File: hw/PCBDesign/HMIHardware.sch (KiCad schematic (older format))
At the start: 24 parts

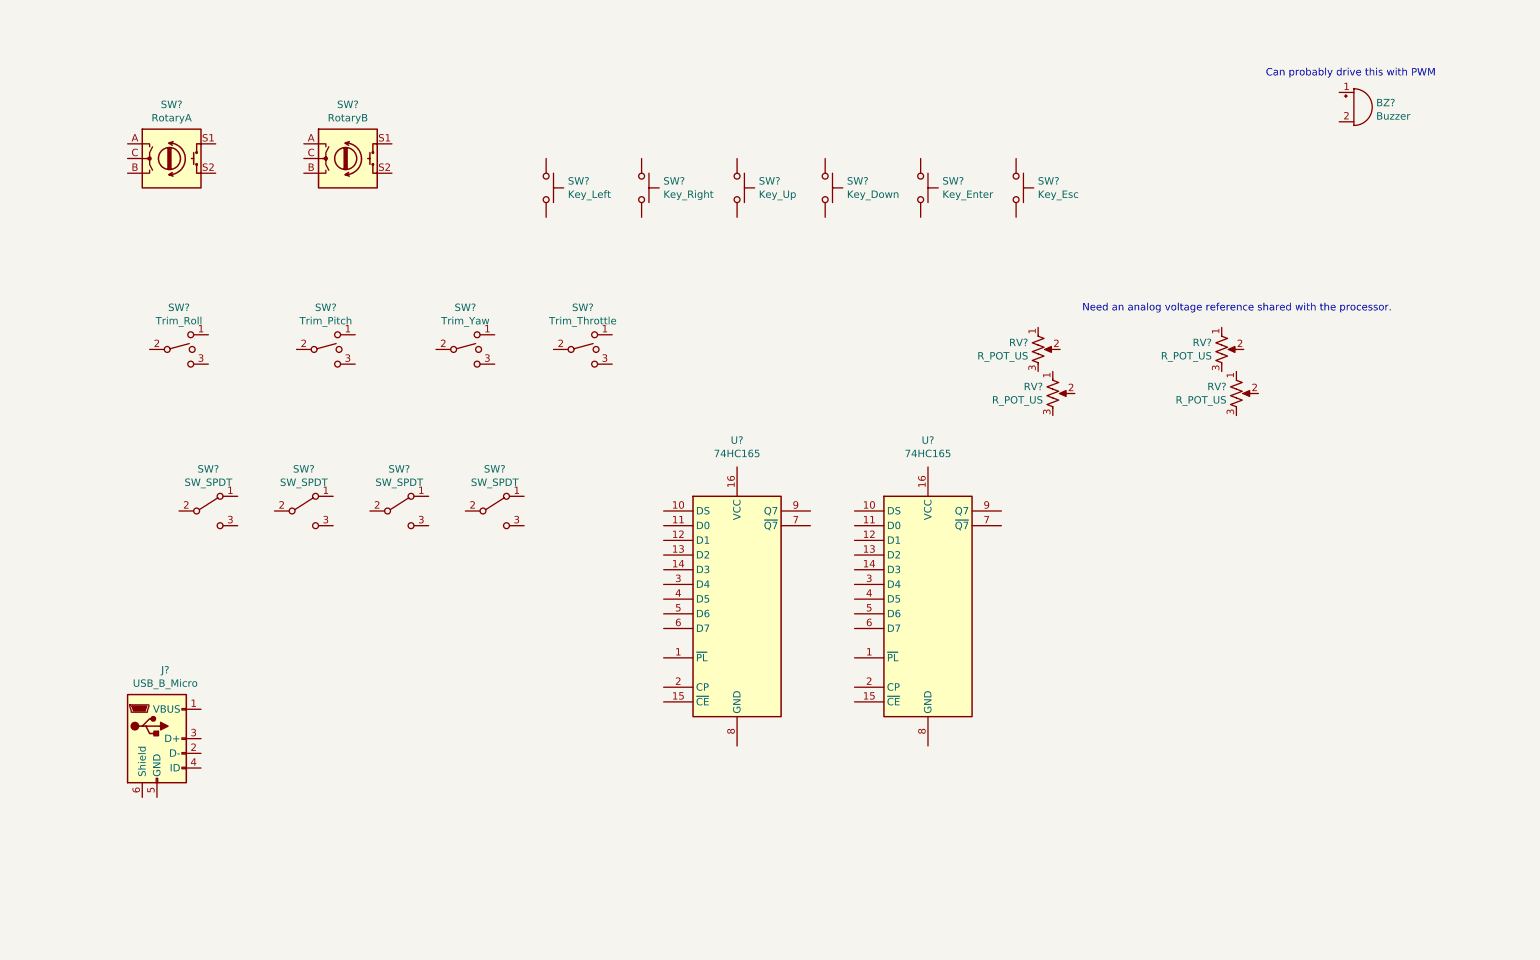
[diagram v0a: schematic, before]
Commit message: Fill out a lot of the board schematic
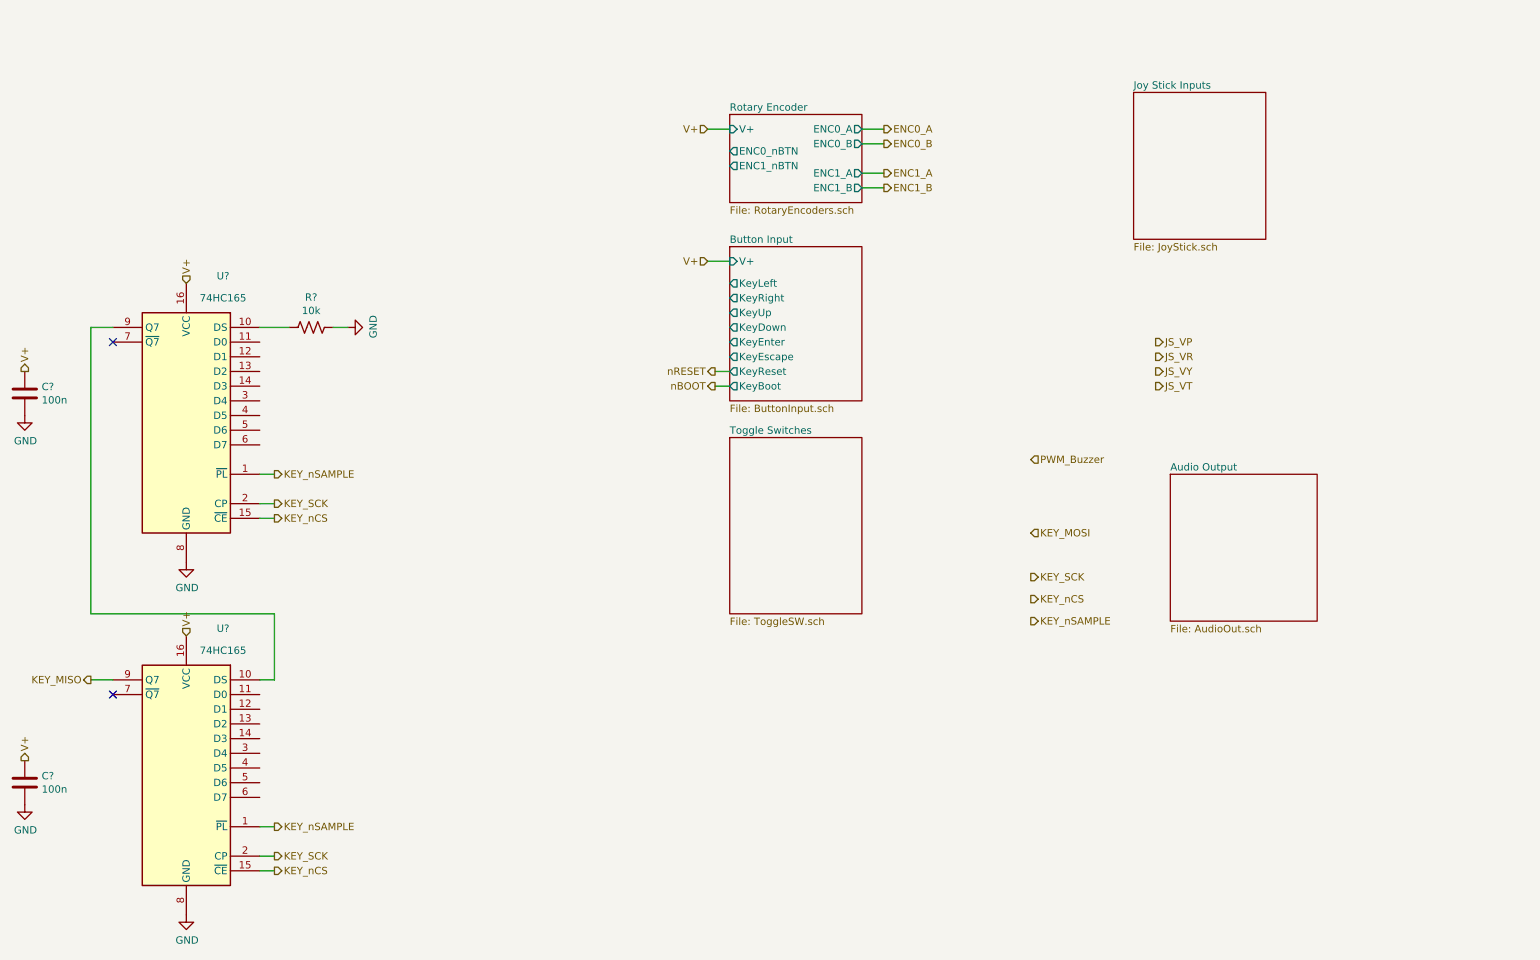
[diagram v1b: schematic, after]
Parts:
- removed BZ?: Buzzer, symbol Device:Buzzer
- removed J?: USB_B_Micro, symbol Connector:USB_B_Micro
- removed RV? (x4): R_POT_US, symbol Device:R_POT_US
- removed SW?: RotaryA, symbol Device:Rotary_Encoder_Switch
- removed SW?: RotaryB, symbol Device:Rotary_Encoder_Switch
- removed SW?: Trim_Roll, symbol Switch:SW_SPDT_MSM
- removed SW?: Trim_Pitch, symbol Switch:SW_SPDT_MSM
- removed SW?: Trim_Yaw, symbol Switch:SW_SPDT_MSM
- removed SW?: Trim_Throttle, symbol Switch:SW_SPDT_MSM
- removed SW?: Key_Left, symbol Switch:SW_Push
- removed SW?: Key_Right, symbol Switch:SW_Push
- removed SW?: Key_Up, symbol Switch:SW_Push
- removed SW?: Key_Down, symbol Switch:SW_Push
- removed SW?: Key_Enter, symbol Switch:SW_Push
- removed SW?: Key_Esc, symbol Switch:SW_Push
- removed SW? (x4): SW_SPDT, symbol Switch:SW_SPDT
- added C? (x2): 100n, symbol Device:C
- added R?: 10k, symbol Device:R_US
- U? (x2): footprint (none) -> Package_SO:SOIC-16_3.9x9.9mm_P1.27mm; LCSC (none) -> C5613
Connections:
- net KEY_nSAMPLE: now reaches U?.1 (~PL)
- net KEY_nSAMPLE: now also U?.1 (~PL)
- net at U?.10 (DS): now also R?.1
- net KEY_nCS: now reaches U?.15 (~CE)
- net KEY_nCS: now also U?.15 (~CE)
- net V+: now reaches U?.16 (VCC)
- net V+: now also U?.16 (VCC), C?.1, C?.1
- net KEY_SCK: now reaches U?.2 (CP)
- net KEY_SCK: now also U?.2 (CP)
- net GND: now reaches U?.8 (GND)
- net GND: now also U?.8 (GND), C?.2, C?.2, R?.2
- net at U?.9 (Q7): now also U?.10 (DS)
- net KEY_MISO: now reaches U?.9 (Q7)
- no-connect marks 0 -> 2
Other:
- note removed: "Can probably drive this with PWM\n"
- note removed: "Need an analog voltage reference shared with the processor."
- moved on the sheet: U?

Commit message: Add HMI input circuitry
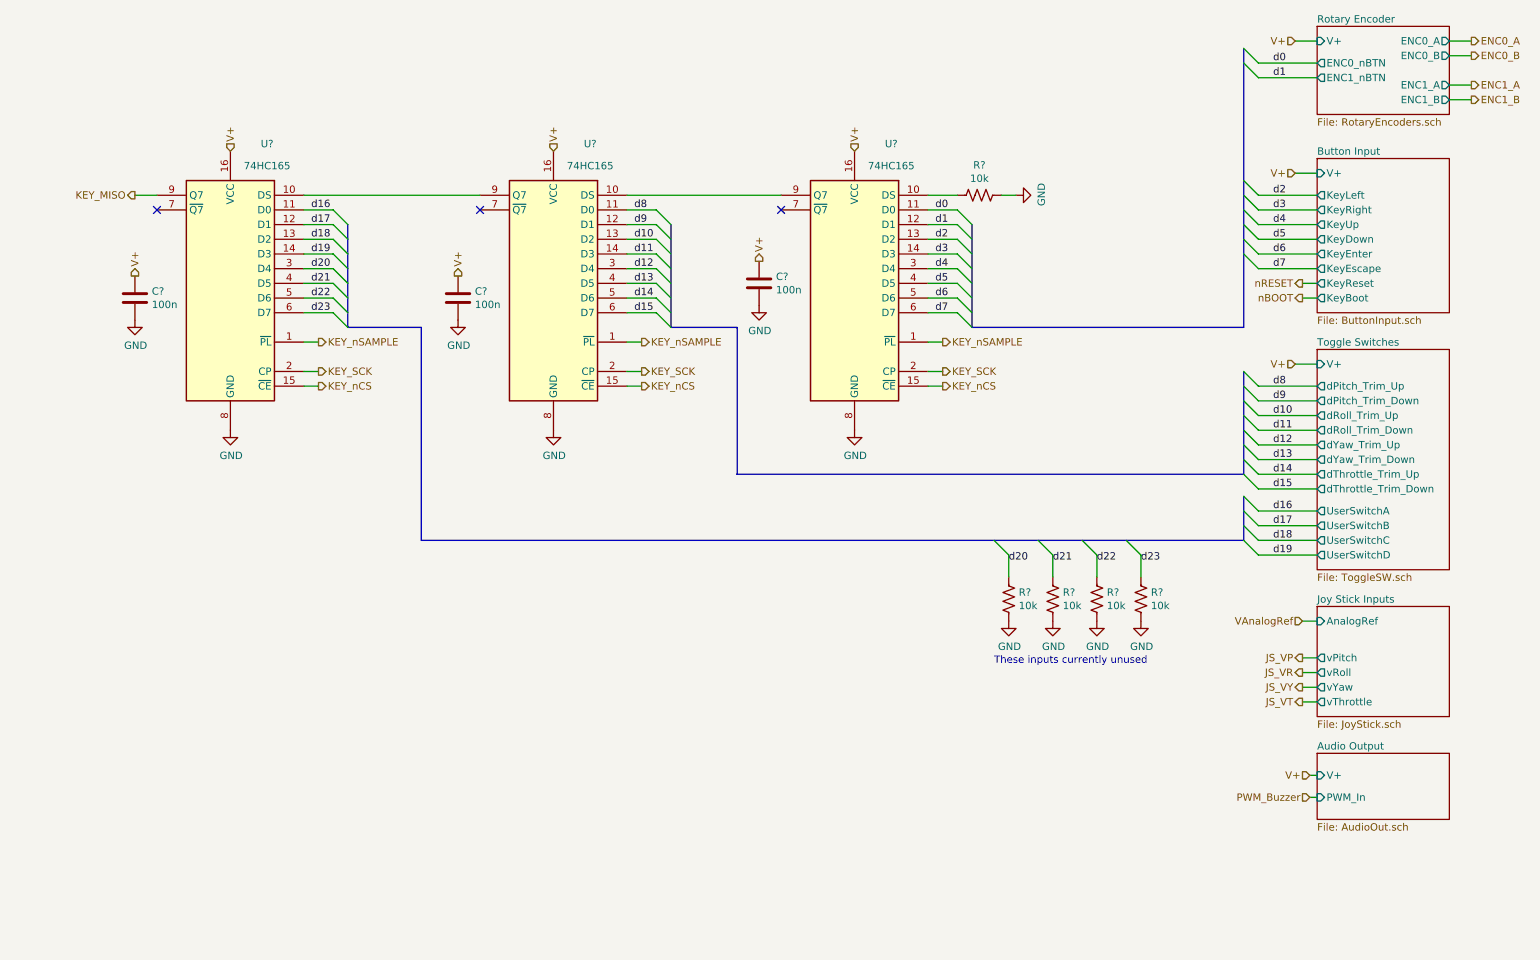
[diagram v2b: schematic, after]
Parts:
- added C?: 100n, symbol Device:C
- added R? (x4): 10k, symbol Device:R_US
- added U?: 74HC165, Package_SO:SOIC-16_3.9x9.9mm_P1.27mm, symbol 74xx:74HC165
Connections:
- net GND: now also C?.2, R?.2, R?.2, R?.2, R?.2, U?.8 (GND)
- net KEY_SCK: now also U?.2 (CP)
- net KEY_nCS: now also U?.15 (~CE)
- net KEY_nSAMPLE: now also U?.1 (~PL)
- net V+: now also C?.1, U?.16 (VCC)
- net d0: now reaches U?.11 (D0)
- net d1: now reaches U?.12 (D1)
- net d2: now reaches U?.13 (D2)
- net d3: now reaches U?.14 (D3)
- net d4: now reaches U?.3 (D4)
- net d5: now reaches U?.4 (D5)
- net d6: now reaches U?.5 (D6)
- net d7: now reaches U?.6 (D7)
- net at U?.9 (Q7): now also U?.10 (DS); no longer U?.10 (DS)
- net d16: now reaches U?.11 (D0)
- net d17: now reaches U?.12 (D1)
- net d18: now reaches U?.13 (D2)
- net d19: now reaches U?.14 (D3)
- net d20: now reaches U?.3 (D4)
- net d20: now also R?.1
- net d21: now reaches U?.4 (D5)
- net d21: now also R?.1
- net d22: now reaches U?.5 (D6)
- net d22: now also R?.1
- net d23: now reaches U?.6 (D7)
- net d23: now also R?.1
- new net: U?.10 (DS), U?.9 (Q7)
- new net d10: U?.13 (D2)
- new net d11: U?.14 (D3)
- new net d12: U?.3 (D4)
- new net d13: U?.4 (D5)
- new net d14: U?.5 (D6)
- new net d15: U?.6 (D7)
- new net d8: U?.11 (D0)
- new net d9: U?.12 (D1)
- no-connect marks 2 -> 3
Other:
- note added: "These inputs currently unused"
- moved on the sheet: C?, R?, U?

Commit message: Finished initial schematic design
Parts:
- removed R? (x2): 10k, symbol Device:R_US
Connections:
- net d20 renamed nBatteryPowerGood
- net d21 renamed nBatteryChargeGood
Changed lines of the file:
@@
-$Comp
-L Device:R_US R?
-U 1 1 605874BC
-P 7500 4650
-F 0 "R?" H 7568 4696 50  0000 L CNN
-F 1 "10k" H 7568 4605 50  0000 L CNN
-F 2 "" V 7540 4640 50  0001 C CNN
-F 3 "~" H 7500 4650 50  0001 C CNN
-	1    7500 4650
-	1    0    0    -1
-$EndComp
-$Comp
-L Device:R_US R?
-U 1 1 60587B6F
-P 7800 4650
-F 0 "R?" H 7868 4696 50  0000 L CNN
-F 1 "10k" H 7868 4605 50  0000 L CNN
-F 2 "" V 7840 4640 50  0001 C CNN
-F 3 "~" H 7800 4650 50  0001 C CNN
-	1    7800 4650
-	1    0    0    -1
-$EndComp
 $Comp
 L Device:R_US R?
@@
 F 3 "~" H 8400 4650 50  0001 C CNN
 	1    8400 4650
-	1    0    0    -1
-$EndComp
-$Comp
-L power:GND #PWR?
-U 1 1 6058901C
-P 7500 4800
-F 0 "#PWR?" H 7500 4550 50  0001 C CNN
-F 1 "GND" H 7505 4627 50  0000 C CNN
-F 2 "" H 7500 4800 50  0001 C CNN
-F 3 "" H 7500 4800 50  0001 C CNN
-	1    7500 4800
-	1    0    0    -1
-$EndComp
-$Comp
-L power:GND #PWR?
-U 1 1 6058949C
-P 7800 4800
-F 0 "#PWR?" H 7800 4550 50  0001 C CNN
-F 1 "GND" H 7805 4627 50  0000 C CNN
-F 2 "" H 7800 4800 50  0001 C CNN
-F 3 "" H 7800 4800 50  0001 C CNN
-	1    7800 4800
 	1    0    0    -1
 $EndComp
@@
 Text Label 8400 4400 0    50   ~ 0
 d23
+Text Notes 8700 5550 1    50   ~ 0
+These inputs currently unused
+Text GLabel 7500 4500 3    50   Output ~ 0
+nBatteryPowerGood
+Text GLabel 7800 4500 3    50   Output ~ 0
+nBatteryChargeGood
 Wire Bus Line
 	9100 3950 9100 4250
@@
 Wire Bus Line
 	9100 900  9100 2800
-Text Notes 7400 5100 0    50   ~ 0
-These inputs currently unused
 $EndSCHEMATC

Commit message: Schematic polishing
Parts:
- removed R?: 10k, symbol Device:R_US
- C1, C2, C3: renamed from C?; footprint (none) -> Capacitor_SMD:C_0402_1005Metric; LCSC (none) -> C1525
- R1, R2: renamed from R?; footprint (none) -> Resistor_SMD:R_0402_1005Metric; LCSC (none) -> C25744
- gave numbers to parts that had none: 3
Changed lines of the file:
@@
 $EndDescr
 $Comp
-L 74xx:74HC165 U?
+L 74xx:74HC165 U3
 U 1 1 60465132
 P 6450 2500
-F 0 "U?" H 6200 3450 50  0000 C CNN
+F 0 "U3" H 6200 3450 50  0000 C CNN
 F 1 "74HC165" H 6200 3300 50  0000 C CNN
 F 2 "Package_SO:SOIC-16_3.9x9.9mm_P1.27mm" H 6450 2500 50  0001 C CNN
@@
 Text HLabel 9450 1750 0    50   Input ~ 0
 V+
-Text HLabel 9500 2600 0    50   Output ~ 0
-nBOOT
 Text HLabel 9500 2500 0    50   Output ~ 0
 nRESET
 $Comp
-L power:GND #PWR?
+L power:GND #PWR018
 U 1 1 6066FFA2
 P 6450 3500
-F 0 "#PWR?" H 6450 3250 50  0001 C CNN
+F 0 "#PWR018" H 6450 3250 50  0001 C CNN
 F 1 "GND" H 6455 3327 50  0000 C CNN
 F 2 "" H 6450 3500 50  0001 C CNN
@@
 NoConn ~ 5950 2000
 $Comp
-L Device:R_US R?
+L Device:R_US R1
 U 1 1 60672EC3
 P 7300 1900
-F 0 "R?" V 7505 1900 50  0000 C CNN
+F 0 "R1" V 7505 1900 50  0000 C CNN
 F 1 "10k" V 7414 1900 50  0000 C CNN
-F 2 "" V 7340 1890 50  0001 C CNN
+F 2 "Resistor_SMD:R_0402_1005Metric" V 7340 1890 50  0001 C CNN
 F 3 "~" H 7300 1900 50  0001 C CNN
+F 4 "C25744" H 7300 1900 50  0001 C CNN "LCSC"
 	1    7300 1900
 	0    -1   -1   0
 $EndComp
 $Comp
-L power:GND #PWR?
+L power:GND #PWR019
 U 1 1 60672ECA
 P 7550 1900
-F 0 "#PWR?" H 7550 1650 50  0001 C CNN
+F 0 "#PWR019" H 7550 1650 50  0001 C CNN
 F 1 "GND" H 7555 1727 50  0000 C CNN
 F 2 "" H 7550 1900 50  0001 C CNN
@@
 V+
 $Comp
-L Device:C C?
+L Device:C C3
 U 1 1 60673CDD
 P 5800 2500
-F 0 "C?" H 5915 2546 50  0000 L CNN
+F 0 "C3" H 5915 2546 50  0000 L CNN
 F 1 "100n" H 5915 2455 50  0000 L CNN
-F 2 "" H 5838 2350 50  0001 C CNN
+F 2 "Capacitor_SMD:C_0402_1005Metric" H 5838 2350 50  0001 C CNN
 F 3 "~" H 5800 2500 50  0001 C CNN
+F 4 "C1525" H 5800 2500 50  0001 C CNN "LCSC"
 	1    5800 2500
 	1    0    0    -1
 $EndComp
 $Comp
-L power:GND #PWR?
+L power:GND #PWR017
 U 1 1 6067404D
 P 5800 2650
-F 0 "#PWR?" H 5800 2400 50  0001 C CNN
+F 0 "#PWR017" H 5800 2400 50  0001 C CNN
 F 1 "GND" H 5805 2477 50  0000 C CNN
 F 2 "" H 5800 2650 50  0001 C CNN
@@
 	9450 1750 9600 1750
 Wire Wire Line
-	9500 2600 9600 2600
-Wire Wire Line
 	9500 2500 9600 2500
 Text HLabel 9500 4800 0    50   Input ~ 0
@@
 	9450 3050 9600 3050
 $Comp
-L power:GND #PWR?
+L power:GND #PWR013
 U 1 1 60675465
 P 1550 2750
-F 0 "#PWR?" H 1550 2500 50  0001 C CNN
+F 0 "#PWR013" H 1550 2500 50  0001 C CNN
 F 1 "GND" H 1555 2577 50  0000 C CNN
 F 2 "" H 1550 2750 50  0001 C CNN
@@
 $EndComp
 $Comp
-L Device:C C?
+L Device:C C1
 U 1 1 6067545F
 P 1550 2600
-F 0 "C?" H 1665 2646 50  0000 L CNN
+F 0 "C1" H 1665 2646 50  0000 L CNN
 F 1 "100n" H 1665 2555 50  0000 L CNN
-F 2 "" H 1588 2450 50  0001 C CNN
+F 2 "Capacitor_SMD:C_0402_1005Metric" H 1588 2450 50  0001 C CNN
 F 3 "~" H 1550 2600 50  0001 C CNN
+F 4 "C1525" H 1550 2600 50  0001 C CNN "LCSC"
 	1    1550 2600
 	1    0    0    -1
@@
 V+
 $Comp
-L power:GND #PWR?
+L power:GND #PWR014
 U 1 1 606707FE
 P 2200 3500
-F 0 "#PWR?" H 2200 3250 50  0001 C CNN
+F 0 "#PWR014" H 2200 3250 50  0001 C CNN
 F 1 "GND" H 2205 3327 50  0000 C CNN
 F 2 "" H 2200 3500 50  0001 C CNN
@@
 KEY_MISO
 $Comp
-L 74xx:74HC165 U?
+L 74xx:74HC165 U1
 U 1 1 6046592A
 P 2200 2500
-F 0 "U?" H 1950 3450 50  0000 C CNN
+F 0 "U1" H 1950 3450 50  0000 C CNN
 F 1 "74HC165" H 1950 3300 50  0000 C CNN
 F 2 "Package_SO:SOIC-16_3.9x9.9mm_P1.27mm" H 2200 2500 50  0001 C CNN
@@
 $EndComp
 $Comp
-L power:GND #PWR?
+L power:GND #PWR015
 U 1 1 60500016
 P 3750 2750
-F 0 "#PWR?" H 3750 2500 50  0001 C CNN
+F 0 "#PWR015" H 3750 2500 50  0001 C CNN
 F 1 "GND" H 3755 2577 50  0000 C CNN
 F 2 "" H 3750 2750 50  0001 C CNN
@@
 $EndComp
 $Comp
-L Device:C C?
+L Device:C C2
 U 1 1 6050001C
 P 3750 2600
-F 0 "C?" H 3865 2646 50  0000 L CNN
+F 0 "C2" H 3865 2646 50  0000 L CNN
 F 1 "100n" H 3865 2555 50  0000 L CNN
-F 2 "" H 3788 2450 50  0001 C CNN
+F 2 "Capacitor_SMD:C_0402_1005Metric" H 3788 2450 50  0001 C CNN
 F 3 "~" H 3750 2600 50  0001 C CNN
+F 4 "C1525" H 3750 2600 50  0001 C CNN "LCSC"
 	1    3750 2600
 	1    0    0    -1
@@
 V+
 $Comp
-L power:GND #PWR?
+L power:GND #PWR016
 U 1 1 6050002C
 P 4400 3500
-F 0 "#PWR?" H 4400 3250 50  0001 C CNN
+F 0 "#PWR016" H 4400 3250 50  0001 C CNN
 F 1 "GND" H 4405 3327 50  0000 C CNN
 F 2 "" H 4400 3500 50  0001 C CNN
@@
 $EndComp
 $Comp
-L 74xx:74HC165 U?
+L 74xx:74HC165 U2
 U 1 1 60500034
 P 4400 2500
-F 0 "U?" H 4150 3450 50  0000 C CNN
+F 0 "U2" H 4150 3450 50  0000 C CNN
 F 1 "74HC165" H 4150 3300 50  0000 C CNN
 F 2 "Package_SO:SOIC-16_3.9x9.9mm_P1.27mm" H 4400 2500 50  0001 C CNN
@@
 	2900 2400 3000 2500
 $Comp
-L Device:R_US R?
-U 1 1 6058828C
-P 8100 4650
-F 0 "R?" H 8168 4696 50  0000 L CNN
-F 1 "10k" H 8168 4605 50  0000 L CNN
-F 2 "" V 8140 4640 50  0001 C CNN
-F 3 "~" H 8100 4650 50  0001 C CNN
-	1    8100 4650
-	1    0    0    -1
-$EndComp
-$Comp
-L Device:R_US R?
+L Device:R_US R2
 U 1 1 60588674
 P 8400 4650
-F 0 "R?" H 8468 4696 50  0000 L CNN
+F 0 "R2" H 8468 4696 50  0000 L CNN
 F 1 "10k" H 8468 4605 50  0000 L CNN
-F 2 "" V 8440 4640 50  0001 C CNN
+F 2 "Resistor_SMD:R_0402_1005Metric" V 8440 4640 50  0001 C CNN
 F 3 "~" H 8400 4650 50  0001 C CNN
+F 4 "C25744" H 8400 4650 50  0001 C CNN "LCSC"
 	1    8400 4650
 	1    0    0    -1
 $EndComp
 $Comp
-L power:GND #PWR?
-U 1 1 60589895
-P 8100 4800
-F 0 "#PWR?" H 8100 4550 50  0001 C CNN
-F 1 "GND" H 8105 4627 50  0000 C CNN
-F 2 "" H 8100 4800 50  0001 C CNN
-F 3 "" H 8100 4800 50  0001 C CNN
-	1    8100 4800
-	1    0    0    -1
-$EndComp
-$Comp
-L power:GND #PWR?
+L power:GND #PWR020
 U 1 1 60589A9A
 P 8400 4800
-F 0 "#PWR?" H 8400 4550 50  0001 C CNN
+F 0 "#PWR020" H 8400 4550 50  0001 C CNN
 F 1 "GND" H 8405 4627 50  0000 C CNN
 F 2 "" H 8400 4800 50  0001 C CNN
@@
 Wire Wire Line
 	8400 4500 8400 4350
-Wire Wire Line
-	8100 4500 8100 4350
 Wire Wire Line
 	7800 4500 7800 4350
@@
 Text GLabel 7800 4500 3    50   Output ~ 0
 nBatteryChargeGood
+Wire Wire Line
+	9200 2600 9600 2600
+Text Label 9200 2600 0    50   ~ 0
+nBoot
+Wire Wire Line
+	8100 4350 8100 4900
 Wire Bus Line
 	9100 3950 9100 4250
@@
 Wire Bus Line
 	9100 900  9100 2800
+Text Label 8100 4900 1    50   ~ 0
+nBoot
 $EndSCHEMATC
